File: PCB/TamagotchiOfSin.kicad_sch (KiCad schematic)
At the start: 14 parts, among them SW1 SW_Push, SW2 SW_Push, SW3 SW_Push, U2 HS96L03W2C03, U3 DFR0299, U4 XIAO-ESP32-C3-SMD

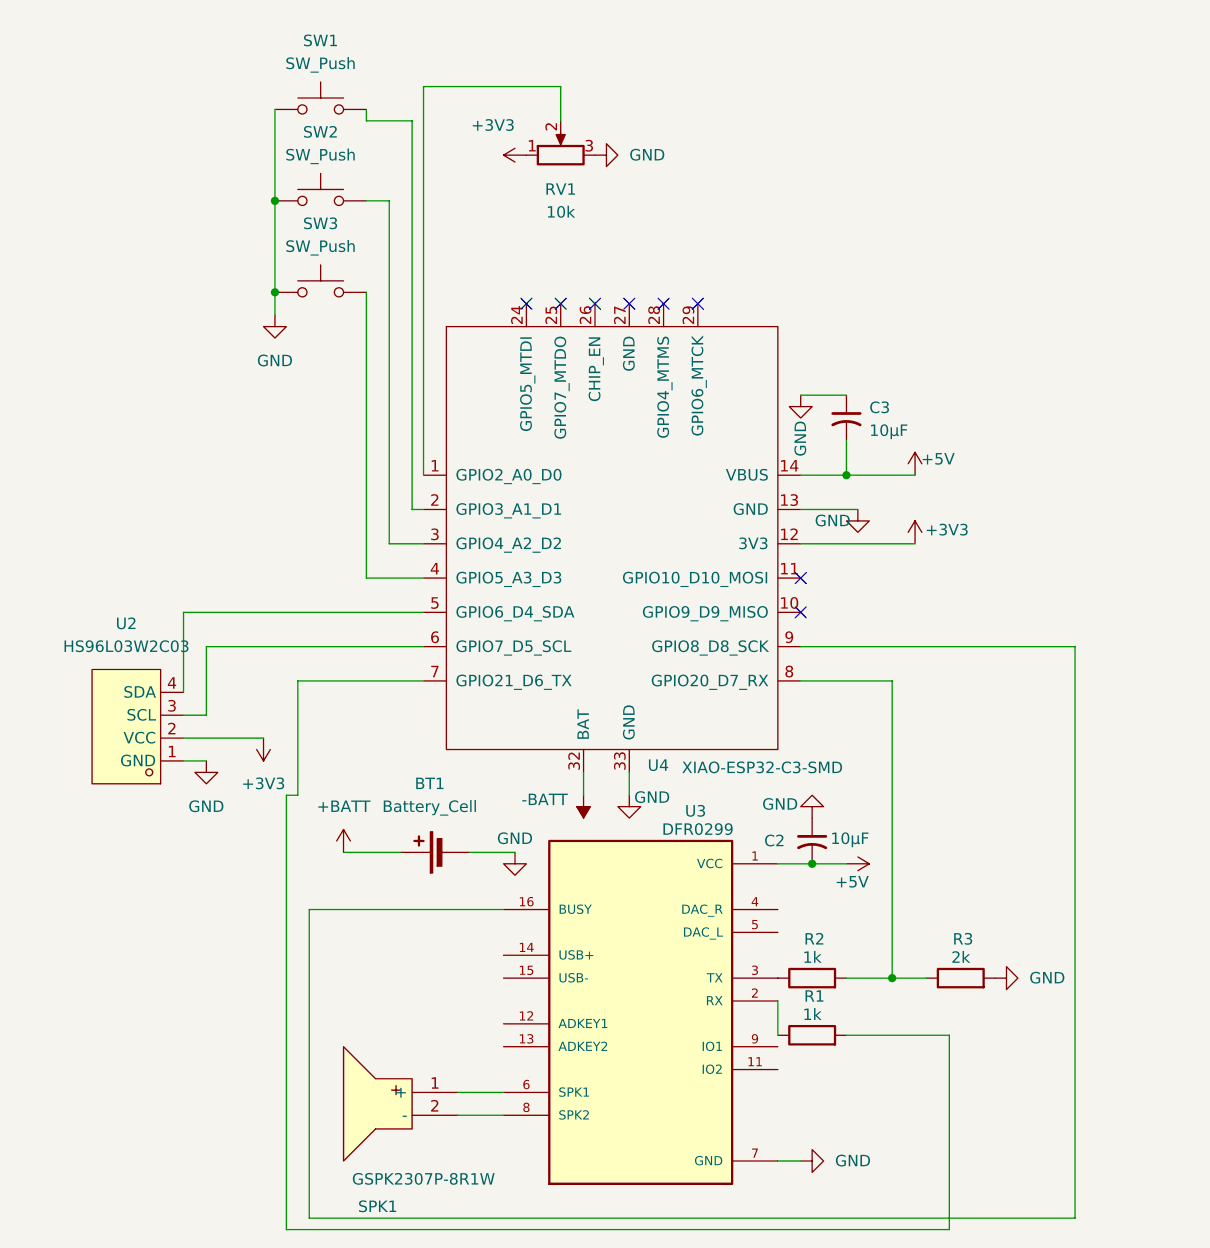
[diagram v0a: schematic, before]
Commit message: updated cad, pcb, not code yet
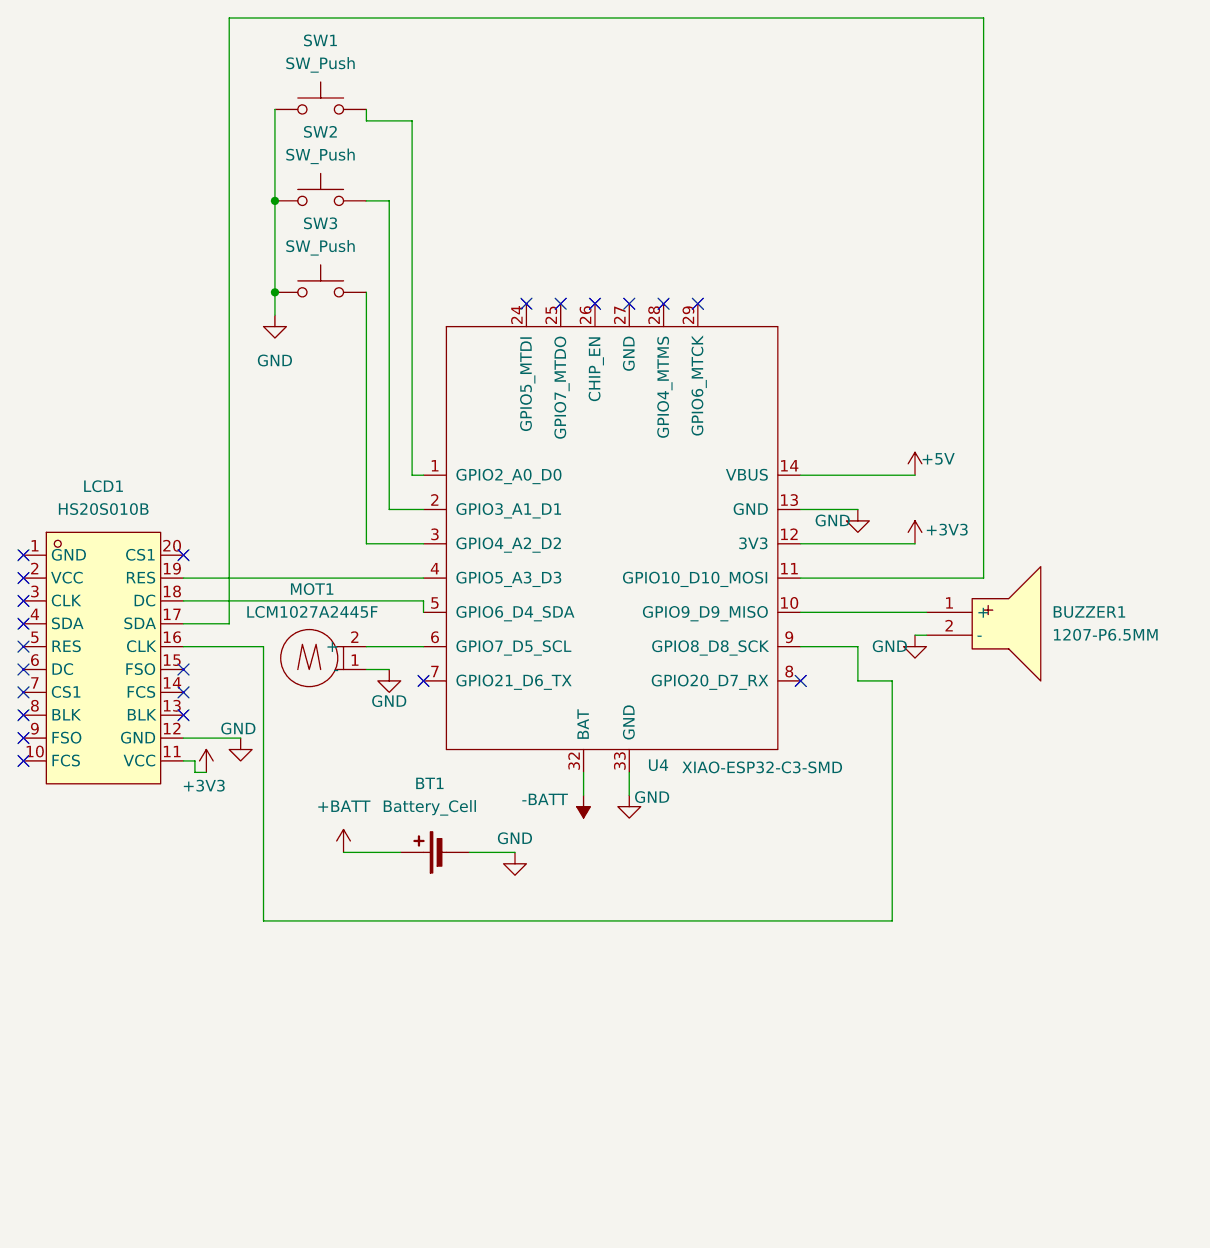
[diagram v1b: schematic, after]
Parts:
- removed C2, C3: 10µF, easyeda2kicad:C0402, symbol Device:C_Small_US
- removed R1, R2: 1k, easyeda2kicad:RES-TH_BD2.7-L6.2-P10.20-D0.4, symbol Device:R
- removed R3: 2k, easyeda2kicad:RES-TH_BD2.3-L6.5-P10.50-D0.5, symbol Device:R
- removed RV1: 10k, easyeda2kicad:RES-ADJ-TH_RK09D1130C3C, symbol Device:R_Potentiometer
- removed SPK1: GSPK2307P-8R1W, easyeda2kicad:SPK-TH_BD23.0-P10.00-D0.8-L-RD, symbol easyeda2kicad:GSPK2307P-8R1W
- removed U2: HS96L03W2C03, easyeda2kicad:OLED-TH_L27.8-W27.2-P2.54_C9900033791, symbol easyeda2kicad:HS96L03W2C03
- removed U3: DFR0299, DFR0299:MODULE_DFR0299, symbol DFR0299:DFR0299
- added BUZZER1: 1207-P6.5MM, easyeda2kicad:BUZ-TH_BD12.5-P6.50-D1.4, symbol easyeda2kicad:1207-P6.5MM
- added LCD1: HS20S010B, easyeda2kicad:LCD-TH_HS20S010B, symbol easyeda2kicad:HS20S010B
- added MOT1: LCM1027A2445F, easyeda2kicad:VIBRATING-MOTOR-SMD_WELDING, symbol easyeda2kicad:LCM1027A2445F
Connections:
- net +3V3: now also LCD1.11 (VCC)
- net GND: now also BUZZER1.2 (-), LCD1.12 (GND), MOT1.1 (-)
- net at U4.9 (GPIO8_D8_SCK): now also LCD1.16 (CLK)
- net at U4.6 (GPIO7_D5_SCL): now also MOT1.2 (+)
- net at U4.5 (GPIO6_D4_SDA): now also LCD1.18 (DC)
- net at U4.4 (GPIO5_A3_D3): now also LCD1.19 (RES); no longer SW3.2
- net at SW1.2: now also U4.1 (GPIO2_A0_D0); no longer U4.2 (GPIO3_A1_D1)
- net at U4.10 (GPIO9_D9_MISO): now also BUZZER1.1 (+)
- net at U4.11 (GPIO10_D10_MOSI): now also LCD1.17 (SDA)
- net at U4.3 (GPIO4_A2_D2): now also SW3.2; no longer SW2.2
- new net: SW2.2, U4.2 (GPIO3_A1_D1)
- no-connect marks 8 -> 22
